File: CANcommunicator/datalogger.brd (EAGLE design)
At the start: 36.8 x 39 mm, 42 parts, among them J1 CORTEX_DEBUG_PTH, U1 ATSAMC21E18A-AU, U2 TXB0104, U3 MCP2551, U4 DS1307Z, Y1 32.768kHz, Y2 32.768kHz

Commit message: I'm an idiot
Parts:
- turned C10 to 180 degrees
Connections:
- net GND: now also U3.2; no longer U3.3
- net VCC: now also U3.3; no longer U3.2
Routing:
- net VCC: track 103.9 -> 100.8 mm
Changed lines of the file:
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@@
 <attribute name="VALUE" x="8.89" y="15.24" size="0.6096" layer="27" font="vector" ratio="20" rot="R90" align="bottom-center"/>
 </element>
-<element name="C10" library="SparkFun-Capacitors" library_urn="urn:adsk.eagle:library:510" package="0603" package3d_urn="urn:adsk.eagle:package:37414/1" value="0.1uF" x="5.334" y="14.478" smashed="yes" rot="MR0">
-<attribute name="NAME" x="5.334" y="15.24" size="0.6096" layer="26" font="vector" ratio="20" rot="MR0" align="bottom-center"/>
-<attribute name="PROD_ID" value="CAP-00810" x="-13.716" y="-41.402" size="1.778" layer="28" rot="MR0" display="off"/>
-<attribute name="VALUE" x="5.334" y="13.716" size="0.6096" layer="28" font="vector" ratio="20" rot="MR0" align="top-center"/>
+<element name="C10" library="SparkFun-Capacitors" library_urn="urn:adsk.eagle:library:510" package="0603" package3d_urn="urn:adsk.eagle:package:37414/1" value="0.1uF" x="5.334" y="14.478" smashed="yes" rot="MR180">
+<attribute name="NAME" x="5.334" y="13.716" size="0.6096" layer="26" font="vector" ratio="20" rot="MR180" align="bottom-center"/>
+<attribute name="PROD_ID" value="CAP-00810" x="24.384" y="70.358" size="1.778" layer="28" rot="MR180" display="off"/>
+<attribute name="VALUE" x="5.334" y="15.24" size="0.6096" layer="28" font="vector" ratio="20" rot="MR180" align="top-center"/>
 </element>
 <element name="C12" library="SparkFun-Capacitors" library_urn="urn:adsk.eagle:library:510" package="0603" package3d_urn="urn:adsk.eagle:package:37414/1" value="560pF" x="2.54" y="22.86" smashed="yes" rot="MR180">
@@
 <attribute name="VALUE" x="33.02" y="4.318" size="0.6096" layer="28" font="vector" ratio="20" rot="MR0" align="top-center"/>
 </element>
-<element name="R6" library="rcl" library_urn="urn:adsk.eagle:library:334" package="R0603" package3d_urn="urn:adsk.eagle:package:23555/2" value="60" x="2.54" y="25.4" smashed="yes">
+<element name="R6" library="rcl" library_urn="urn:adsk.eagle:library:334" package="R0603" package3d_urn="urn:adsk.eagle:package:23555/3" value="60" x="2.54" y="25.4" smashed="yes">
 <attribute name="NAME" x="1.905" y="26.035" size="1.27" layer="25"/>
 <attribute name="SPICEPREFIX" value="R" x="49.53" y="-24.13" size="1.778" layer="27" display="off"/>
 <attribute name="VALUE" x="1.905" y="23.495" size="1.27" layer="27"/>
 </element>
-<element name="R7" library="rcl" library_urn="urn:adsk.eagle:library:334" package="R0603" package3d_urn="urn:adsk.eagle:package:23555/2" value="120" x="6.35" y="25.4" smashed="yes">
+<element name="R7" library="rcl" library_urn="urn:adsk.eagle:library:334" package="R0603" package3d_urn="urn:adsk.eagle:package:23555/3" value="120" x="6.35" y="25.4" smashed="yes">
 <attribute name="NAME" x="5.715" y="26.035" size="1.27" layer="25"/>
 <attribute name="SPICEPREFIX" value="R" x="44.45" y="-24.13" size="1.778" layer="27" display="off"/>
@@
 <signals>
 <signal name="GND" class="1">
-<contactref element="U3" pad="3"/>
-<contactref element="C10" pad="1"/>
 <contactref element="R8" pad="2"/>
 <contactref element="C13" pad="2"/>
@@
 <via x="22.86" y="7.62" extent="1-16" drill="0.35"/>
 <via x="7.62" y="33.02" extent="1-16" drill="0.35"/>
+<contactref element="C10" pad="1"/>
+<contactref element="U3" pad="2"/>
 </signal>
 <signal name="C1RS">
@@
 </signal>
 <signal name="VCC" class="1">
-<contactref element="U3" pad="2"/>
 <contactref element="C10" pad="2"/>
 <contactref element="C9" pad="1"/>
@@
 <contactref element="IC1" pad="IN"/>
 <contactref element="PWR" pad="1"/>
-<wire x1="11.43" y1="3.81" x2="6.35" y2="8.89" width="0.4064" layer="1"/>
-<wire x1="4.1148" y1="11.1948" x2="4.1148" y2="10.3952" width="0.4064" layer="1"/>
-<wire x1="4.1148" y1="10.3952" x2="4.6802" y2="9.8298" width="0.4064" layer="1"/>
-<wire x1="4.6802" y1="9.8298" x2="5.08" y2="9.8298" width="0.4064" layer="1"/>
-<wire x1="4.445" y1="12.44" x2="4.445" y2="11.525" width="0.4064" layer="1"/>
-<wire x1="4.445" y1="11.525" x2="4.1148" y2="11.1948" width="0.4064" layer="1"/>
-<wire x1="5.08" y1="9.8298" x2="6.0198" y2="8.89" width="0.4064" layer="1"/>
-<wire x1="6.0198" y1="8.89" x2="6.35" y2="8.89" width="0.4064" layer="1"/>
 <wire x1="11.43" y1="3.81" x2="14.56" y2="6.94" width="0.4064" layer="1"/>
 <wire x1="14.56" y1="6.94" x2="14.56" y2="7.9978" width="0.4064" layer="1"/>
 <wire x1="15.24" y1="36.195" x2="15.875" y2="35.56" width="0.4064" layer="1"/>
 <wire x1="15.875" y1="35.56" x2="20.32" y2="35.56" width="0.4064" layer="1"/>
-<wire x1="9.31" y1="11.43" x2="6.77" y2="8.89" width="0.4064" layer="1"/>
-<wire x1="6.77" y1="8.89" x2="6.35" y2="8.89" width="0.4064" layer="1"/>
-<wire x1="4.484" y1="14.478" x2="4.484" y2="11.564" width="0.4064" layer="16"/>
-<wire x1="4.484" y1="11.564" x2="4.1148" y2="11.1948" width="0.4064" layer="16"/>
-<wire x1="4.1148" y1="11.1948" x2="4.1148" y2="10.3952" width="0.4064" layer="16"/>
-<wire x1="4.1148" y1="10.3952" x2="4.6802" y2="9.8298" width="0.4064" layer="16"/>
-<wire x1="4.6802" y1="9.8298" x2="5.4102" y2="9.8298" width="0.4064" layer="16"/>
-<wire x1="5.4102" y1="9.8298" x2="6.35" y2="8.89" width="0.4064" layer="16"/>
 <wire x1="14.56" y1="6.94" x2="15.15" y2="6.35" width="0.4064" layer="1"/>
 <wire x1="15.15" y1="6.35" x2="15.24" y2="6.35" width="0.4064" layer="1"/>
@@
 <wire x1="11.3792" y1="16.5354" x2="11.8237" y2="16.0909" width="0.4064" layer="16"/>
 <wire x1="6.5786" y1="16.5354" x2="11.3792" y2="16.5354" width="0.4064" layer="16"/>
-<wire x1="4.6228" y1="14.5796" x2="6.5786" y2="16.5354" width="0.4064" layer="16"/>
 <wire x1="12.6238" y1="16.0909" x2="12.7" y2="16.09" width="0.4064" layer="16"/>
-<wire x1="4.6228" y1="14.5796" x2="4.484" y2="14.478" width="0.4064" layer="16"/>
+<contactref element="U3" pad="3"/>
+<wire x1="6.184" y1="14.478" x2="6.184" y2="16.1408" width="0.4064" layer="16"/>
+<wire x1="6.184" y1="16.1408" x2="6.5786" y2="16.5354" width="0.4064" layer="16"/>
+<wire x1="11.43" y1="3.81" x2="6.35" y2="8.89" width="0.4064" layer="1"/>
+<wire x1="6.35" y1="8.89" x2="5.715" y2="9.525" width="0.4064" layer="1"/>
+<wire x1="5.715" y1="9.525" x2="5.715" y2="10.065" width="0.4064" layer="1"/>
+<wire x1="5.715" y1="10.065" x2="6.0452" y2="10.3952" width="0.4064" layer="1"/>
+<wire x1="6.0452" y1="10.3952" x2="6.0452" y2="11.1948" width="0.4064" layer="1"/>
+<wire x1="6.0452" y1="11.1948" x2="5.715" y2="11.525" width="0.4064" layer="1"/>
+<wire x1="5.715" y1="11.525" x2="5.715" y2="12.44" width="0.4064" layer="1"/>
+<wire x1="6.35" y1="8.89" x2="8.89" y2="11.43" width="0.4064" layer="1"/>
+<wire x1="8.89" y1="11.43" x2="9.31" y2="11.43" width="0.4064" layer="1"/>
+<wire x1="6.35" y1="8.89" x2="6.184" y2="9.056" width="0.4064" layer="16"/>
+<wire x1="6.184" y1="9.056" x2="6.184" y2="14.478" width="0.4064" layer="16"/>
 </signal>
 <signal name="CAN0TX">

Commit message: moved some stuff
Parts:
- moved C11 12.5 mm to (21.6, 3.81)
- moved C9 12.5 mm to (21.6, 6.35)
- moved IC1 12.0 mm to (16.5, 5.08), turned to 90 degrees
- moved U2 11.5 mm to (27.9, 6.35), turned to 90 degrees
- moved SD1 4.02 mm to (31.8, 11.4)
- moved C7 4.02 mm to (26.7, 30.5)
- moved R12 3.81 mm to (26.7, 27.9)
- moved R1 3.81 mm to (16.5, 27.9)
- moved U4 3.81 mm to (26.7, 22.9)
- moved C1 2.54 mm to (19.7, 30.6)
- moved R4 2.54 mm to (15.2, 30.5)
- moved U1 1.27 mm to (15.2, 16.5)
- moved C4 1.27 mm to (14.0, 24.1)
- moved C5 1.27 mm to (16.5, 24.1)
- moved C8 1.27 mm to (19.1, 24.1)
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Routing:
- net VCC: track 100.8 -> 0.00 mm, vias 3 -> 0
- net CONN0: track 63.1 -> 0.00 mm, vias 3 -> 0
- net 3.3V: track 59.9 -> 0.00 mm, vias 3 -> 0
- net CONN3: track 55.7 -> 0.00 mm, vias 1 -> 0
- net CONN2: track 55.0 -> 0.00 mm
- net CONN1: track 47.8 -> 0.00 mm, vias 1 -> 0
- net CAN0H: track 44.9 -> 0.00 mm, vias 1 -> 0
- net N$1: track 44.9 -> 0.00 mm, vias 5 -> 0
- net SD_CD: track 36.7 -> 0.00 mm, vias 2 -> 0
- net CAN0L: track 36.3 -> 0.00 mm, vias 1 -> 0
- net RADIO0: track 32.2 -> 0.00 mm, vias 1 -> 0
- net RADIO3: track 31.2 -> 0.00 mm, vias 3 -> 0
- net SWDIO: track 30.4 -> 0.00 mm, vias 4 -> 0
- net RESET_L: track 26.5 -> 0.00 mm, vias 3 -> 0
- net RADIO1: track 26.1 -> 0.00 mm, vias 3 -> 0
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
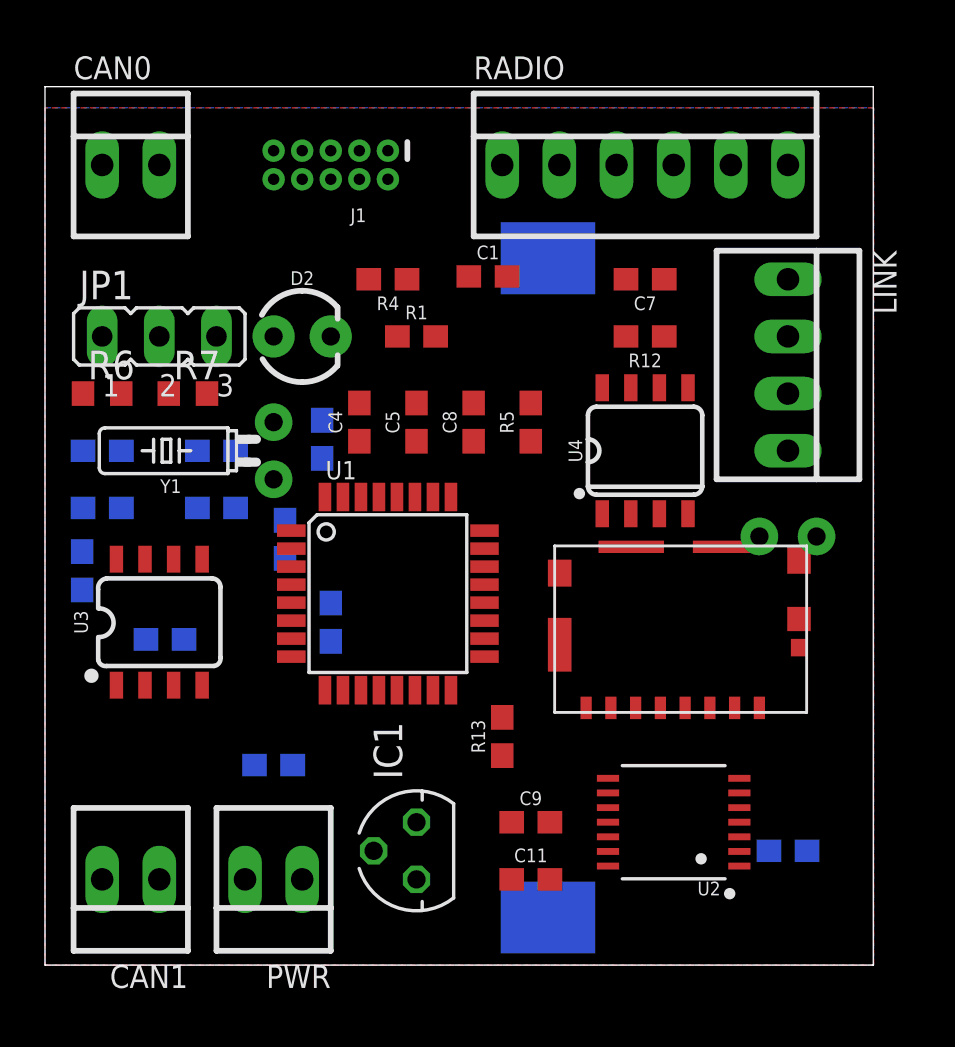
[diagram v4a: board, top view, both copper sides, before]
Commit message: connected ground planes
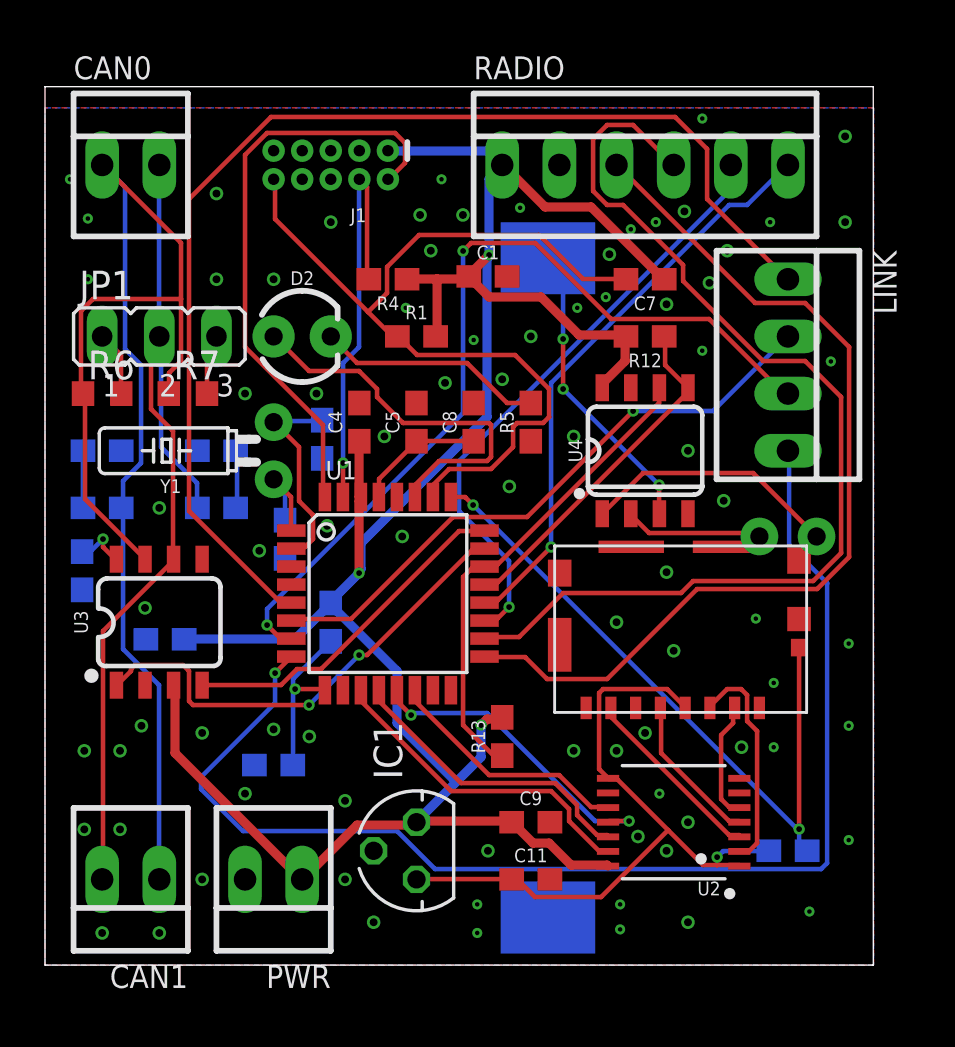
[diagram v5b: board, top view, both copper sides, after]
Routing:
- net VCC: track 0.00 -> 111.2 mm, vias 0 -> 3
- net CAN0H: track 0.00 -> 62.3 mm
- net CONN3: track 0.00 -> 56.0 mm, vias 0 -> 1
- net CONN0: track 0.00 -> 52.5 mm
- net RADIO1: track 0.00 -> 46.5 mm
- net CAN0L: track 0.00 -> 42.0 mm
- net RADIO0: track 0.00 -> 41.9 mm
- net RESET_L: track 0.00 -> 40.2 mm
- net CONN2: track 0.00 -> 38.9 mm, vias 0 -> 2
- net 3.3V: track 0.00 -> 31.2 mm, vias 0 -> 1
- net SD_CD: track 0.00 -> 30.8 mm, vias 0 -> 2
- net CONN1: track 0.00 -> 27.3 mm, vias 0 -> 1
- net RADIO2: track 0.00 -> 27.0 mm, vias 0 -> 1
- net SWDIO: track 0.00 -> 26.4 mm
- net RADIO3: track 0.00 -> 25.8 mm, vias 0 -> 1
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
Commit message: fixed DRC errors
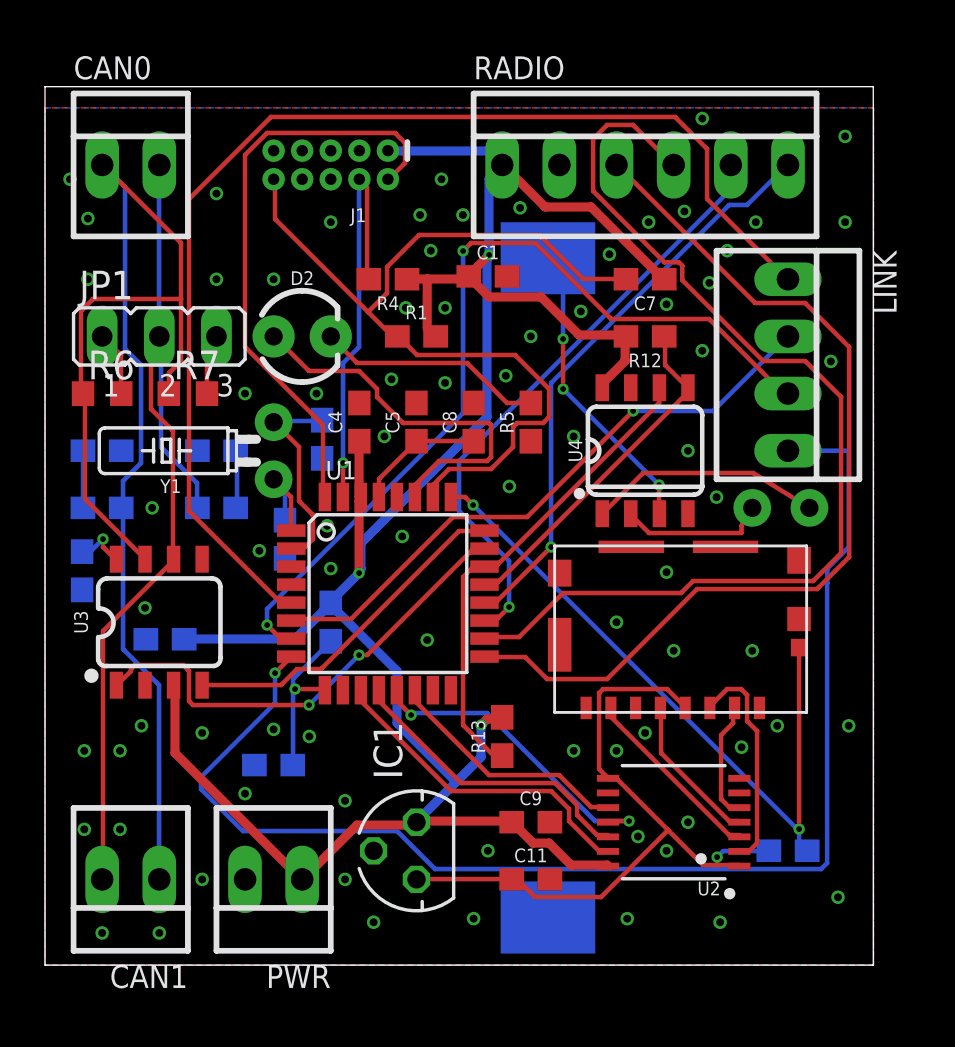
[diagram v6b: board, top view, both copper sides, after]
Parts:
- moved Y2 1.31 mm to (32.7, 20.3)
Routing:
- net CONN3: track 56.0 -> 58.4 mm
- net N$4: track 11.4 -> 10.4 mm
